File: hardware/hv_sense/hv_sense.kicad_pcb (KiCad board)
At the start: 2 copper layers, 69 parts, among them J1 Conn_01x02, J2 Conn_01x02, J3 Conn_01x02, J4 Conn_01x02, J5 Conn_01x03, J6 Conn_01x02, J7 Conn_01x04, U1 4081, U10 140817141410, U2 4071, U3 4081, U4 40106, U5 40106, U6 4013, U8 TLV274, U9 TL431ACDT

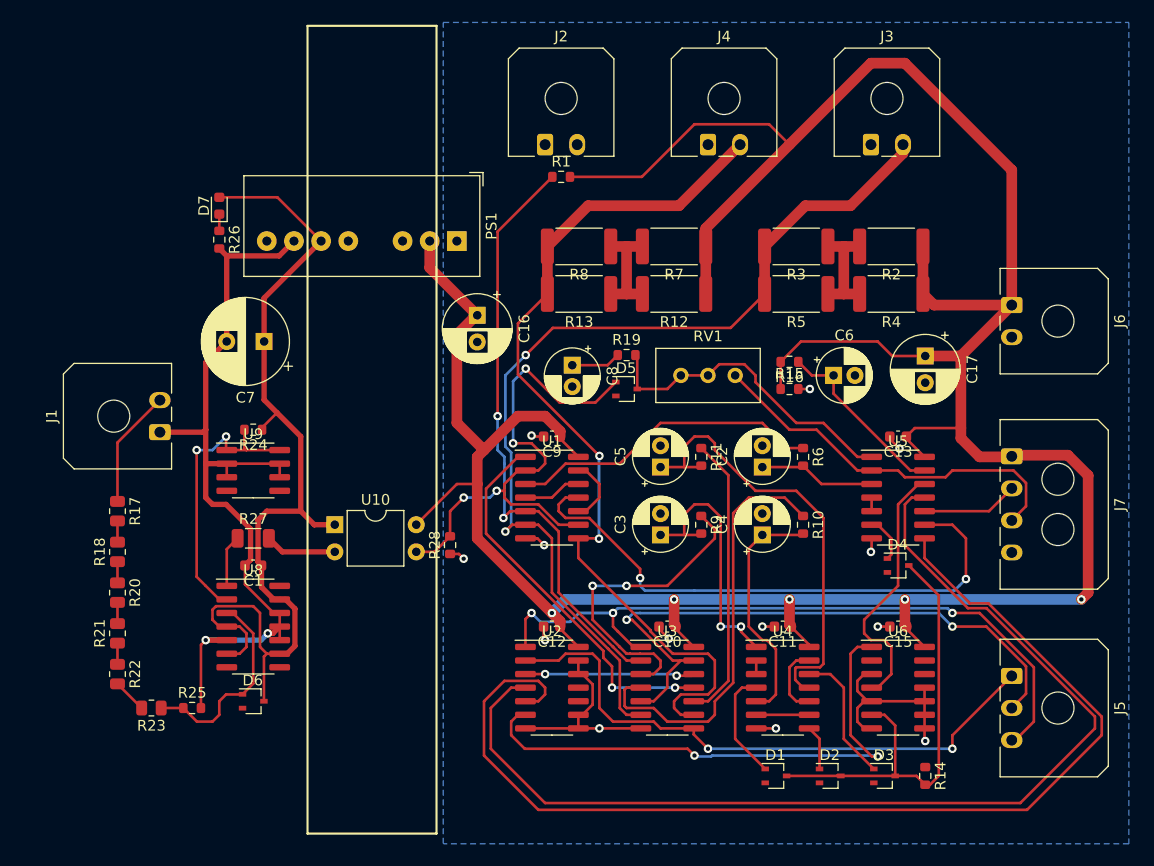
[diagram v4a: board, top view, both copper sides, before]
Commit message: Added edge, moved component references to be visible
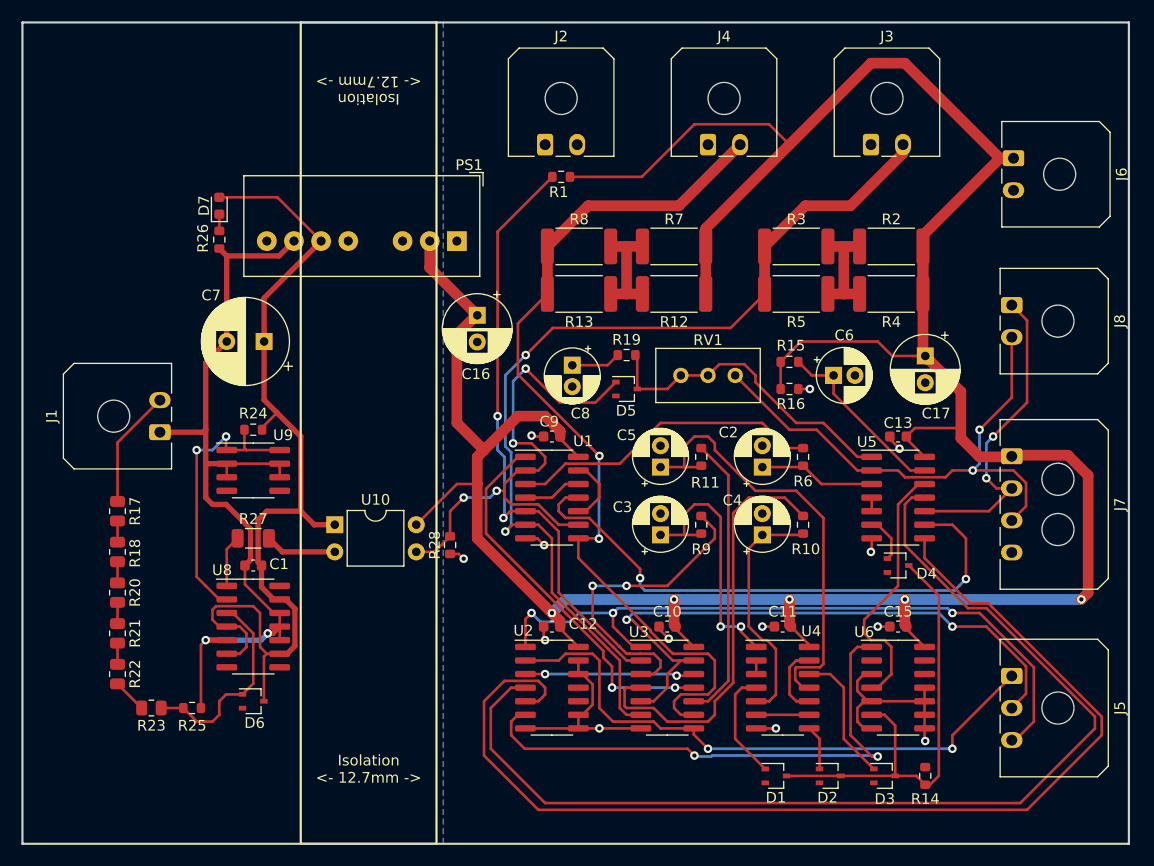
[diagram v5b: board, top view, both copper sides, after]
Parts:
- added J8: Conn_01x02, Connector_Molex:Molex_Micro-Fit_3.0_43650-0200_1x02_P3.00mm_Horizontal, F.Cu at (193.5, 43.6)
- moved J6 13.7 mm to (193.7, 29.8)
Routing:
- net /Implausibility and LED logic/GREEN_LED_ON: track 9.04 -> 30.2 mm, vias 0 -> 2
- net /Implausibility and LED logic/RED_LED_ON: track 36.0 -> 49.9 mm, vias 0 -> 2
- net +12V: track 294.1 -> 285.4 mm
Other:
- board outline added: 103.5 x 76.8 mm
- board text added: "Isolation <- 12.7mm ->"

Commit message: Added mounting holes and TS/LV labels
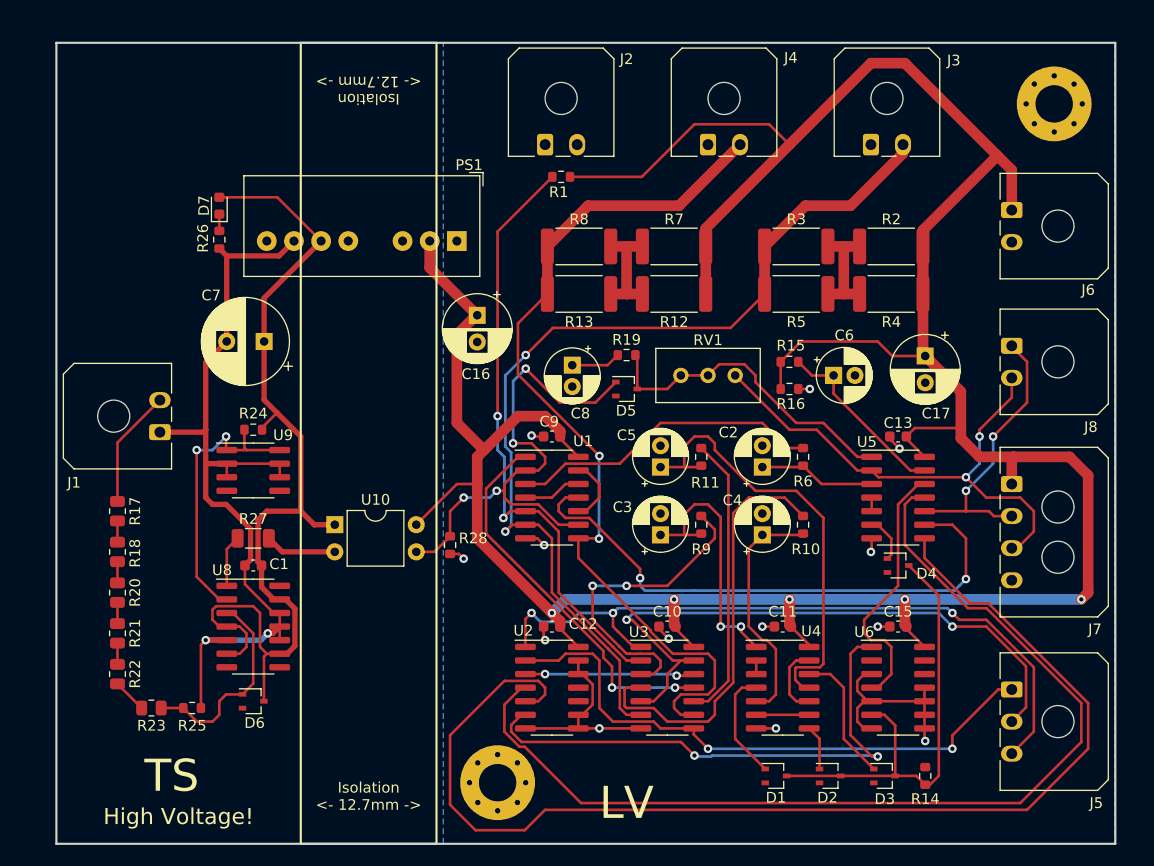
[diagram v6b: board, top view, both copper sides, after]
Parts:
- added REF**: MountingHole_3.5mm_Pad_Via, MountingHole:MountingHole_3.5mm_Pad_Via, F.Cu at (197.5, 24.8)
- added REF**: MountingHole_3.5mm_Pad_Via, MountingHole:MountingHole_3.5mm_Pad_Via, F.Cu at (145.4, 88.3)
- moved J6 4.85 mm to (193.5, 34.7)
- moved J8 3.81 mm to (193.5, 47.4)
- moved J7 2.60 mm to (193.5, 60.3)
- moved J5 1.27 mm to (193.5, 79.5)
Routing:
- net /Implausibility and LED logic/TS_UNSAFE: track 103.7 -> 111.4 mm
- net +12V: track 285.4 -> 293.1 mm
- net Net-(U2-Pad4): track 100.8 -> 96.4 mm
- net /Implausibility and LED logic/GREEN_LED_ON: track 30.2 -> 26.8 mm
- net /LOW_AIR_INTENDED_ON: track 58.1 -> 59.4 mm
- net /PRCHG_INTENDED_ON: track 66.1 -> 67.2 mm
- net /Implausibility and LED logic/RED_LED_ON: track 49.9 -> 48.9 mm
- net /HIGH_AIR_INTENDED_ON: track 55.9 -> 55.4 mm
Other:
- board size 103.5 x 76.8 mm -> 99.1 x 74.9 mm
- board text added: "High Voltage!"
- board text added: "LV"
- board text added: "TS"

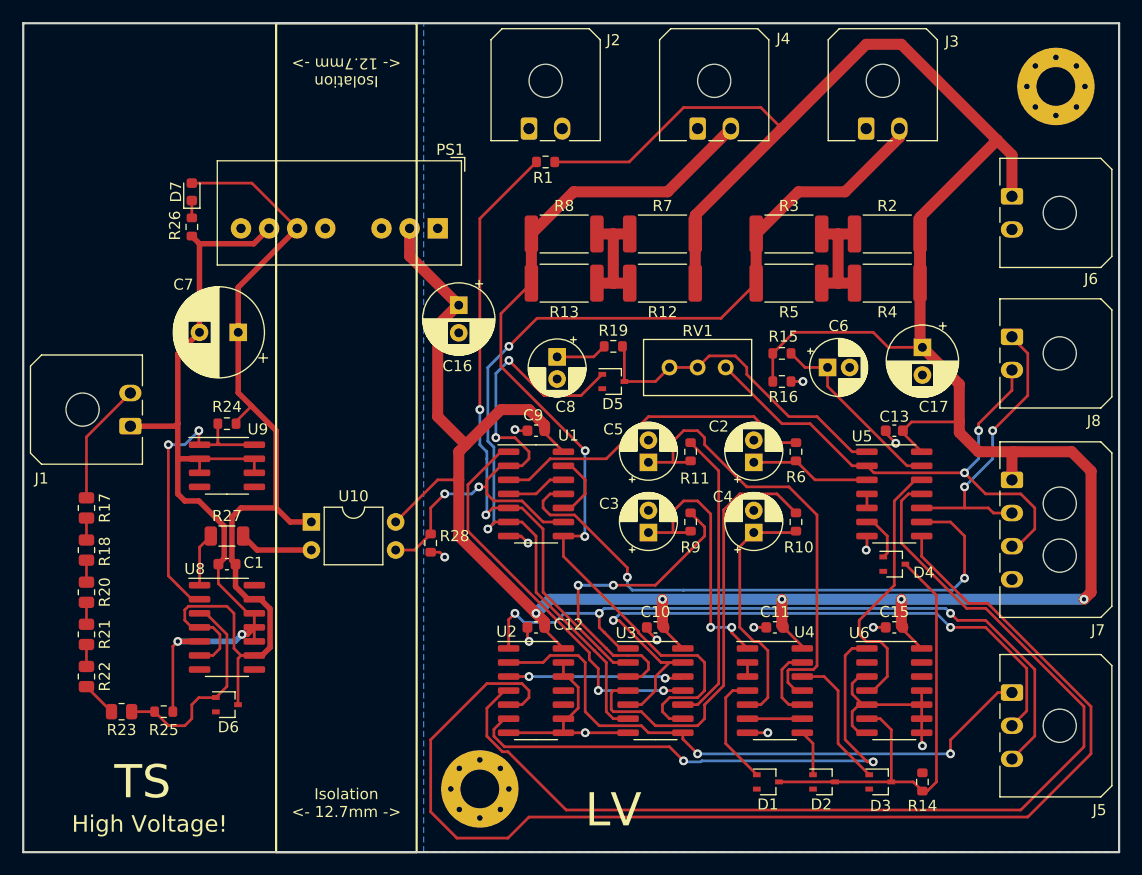
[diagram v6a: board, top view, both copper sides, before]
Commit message: Capped voltage input to opamp
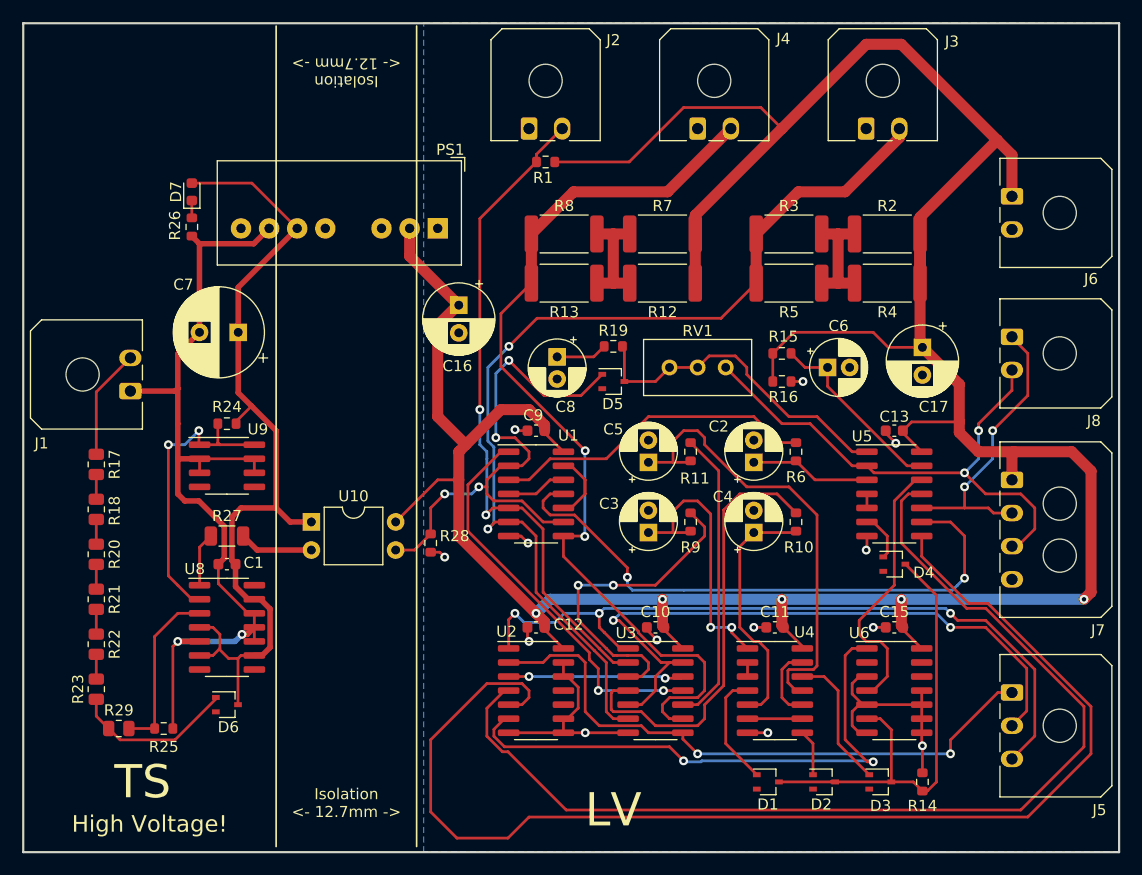
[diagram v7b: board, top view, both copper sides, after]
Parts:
- removed REF** (x2): MountingHole_3.5mm_Pad_Via, MountingHole:MountingHole_3.5mm_Pad_Via
- added R29: 105k, Resistor_SMD:R_0805_2012Metric, F.Cu at (112.8, 82.8)
- R23: value 453k -> 348k
- moved R17 4.04 mm to (110.7, 58.9)
- moved R18 3.79 mm to (110.7, 63.0)
- moved R20 3.54 mm to (110.7, 67.1)
- moved R21 3.30 mm to (110.7, 71.1)
- moved J1 3.18 mm to (113.8, 52.3)
- moved R23 3.06 mm to (110.7, 79.2), turned to 90 degrees
- moved R22 3.05 mm to (110.7, 75.2)
- moved R25 1.52 mm to (116.8, 82.8)
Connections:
- R25 pad 1: Net-(D6-Pad1) -> Net-(R25-Pad1)
- U8 pad 3: Net-(D6-Pad1) -> Net-(R25-Pad1)
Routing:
- net Net-(R25-Pad1): track 0.00 -> 15.6 mm
- net /HV_+12V: track 88.6 -> 79.2 mm
- net Net-(D6-Pad1): track 19.3 -> 14.9 mm
- net /~{PRCHG_MECH_ON}: track 56.6 -> 60.6 mm
- net GND: track 52.9 -> 55.3 mm
- net Net-(J1-Pad2): track 11.1 -> 9.99 mm
- net Net-(R22-Pad2): track 3.20 -> 2.24 mm

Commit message: Changed connector footprints
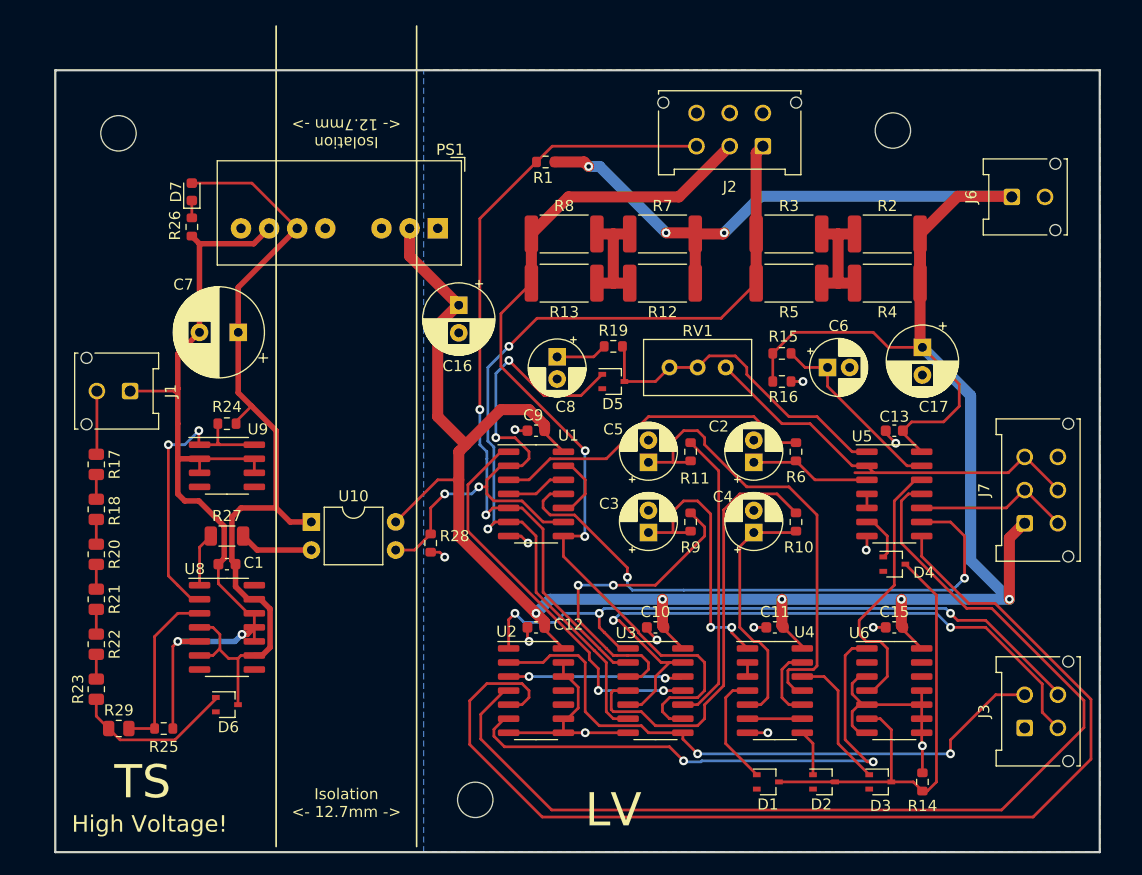
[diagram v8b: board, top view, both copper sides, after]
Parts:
- removed J4, J8: Conn_01x02, Connector_Molex:Molex_Micro-Fit_3.0_43650-0200_1x02_P3.00mm_Horizontal
- removed J5: Conn_01x03, Connector_Molex:Molex_Micro-Fit_3.0_43650-0300_1x03_P3.00mm_Horizontal
- added H1: MountingHole, MountingHole:MountingHole_3.2mm_M3, F.Cu at (112.8, 29.0)
- added H2: MountingHole, MountingHole:MountingHole_3.2mm_M3, F.Cu at (182.8, 28.8)
- added H3: MountingHole, MountingHole:MountingHole_3.2mm_M3, F.Cu at (145.0, 89.2)
- J1, J6: footprint Connector_Molex:Molex_Micro-Fit_3.0_43650-0200_1x02_P3.00mm_Horizontal -> footprints:Molex_Micro-Fit_3.0_43045-0212_2x01_P3.00mm_Vertical
- J2: value Conn_01x02 -> Conn_01x06; footprint Connector_Molex:Molex_Micro-Fit_3.0_43650-0200_1x02_P3.00mm_Horizontal -> footprints:Molex_Micro-Fit_3.0_43045-0612_2x03_P3.00mm_Vertical
- J3: value Conn_01x02 -> Conn_01x04; footprint Connector_Molex:Molex_Micro-Fit_3.0_43650-0200_1x02_P3.00mm_Horizontal -> footprints:Molex_Micro-Fit_3.0_43045-0412_2x02_P3.00mm_Vertical
- J7: value Conn_01x04 -> Conn_01x06; footprint Connector_Molex:Molex_Micro-Fit_3.0_43650-0400_1x04_P3.00mm_Horizontal -> footprints:Molex_Micro-Fit_3.0_43045-0612_2x03_P3.00mm_Vertical
- moved J3 56.0 mm to (194.7, 82.8), turned to 90 degrees
- moved J2 21.2 mm to (171.0, 30.2), turned to 180 degrees
- moved J7 4.09 mm to (194.7, 64.2), turned to 90 degrees
- moved J6 0.06 mm to (193.5, 34.8), turned to 90 degrees
- turned J1 to -90 degrees
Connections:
- J2 pad 1: GND -> /~{LOW_AIR_MECH_ON}
- J2 pad 2: /~{PRCHG_MECH_ON} -> /~{HIGH_AIR_MECH_ON}
- J3 pad 1: GND -> unconnected-(J3-Pad1)
- J3 pad 2: /~{LOW_AIR_MECH_ON} -> /HIGH_AIR_INTENDED_ON
- J7 pad 4: GND -> /Implausibility and LED logic/GREEN_LED_ON
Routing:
- net +12V: track 293.1 -> 266.1 mm, vias 5 -> 8
- net /Implausibility and LED logic/GREEN_LED_ON: track 26.8 -> 14.2 mm, vias 2 -> 0
- net /Implausibility and LED logic/RED_LED_ON: track 48.9 -> 37.5 mm, vias 2 -> 0
- net /~{PRCHG_MECH_ON}: track 60.6 -> 71.6 mm
- net /Implausibility and LED logic/TS_UNSAFE: track 111.4 -> 101.9 mm
- net /~{LOW_AIR_MECH_ON}: track 90.2 -> 81.0 mm
- net /PRCHG_INTENDED_ON: track 67.2 -> 61.4 mm
- net Net-(J1-Pad2): track 9.99 -> 5.74 mm
- net /HIGH_AIR_INTENDED_ON: track 55.4 -> 56.5 mm
- net /LOW_AIR_INTENDED_ON: track 59.4 -> 60.2 mm
- net /~{HIGH_AIR_MECH_ON}: track 83.8 -> 83.1 mm
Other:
- board size 99.1 x 74.9 mm -> 94.4 x 70.7 mm
